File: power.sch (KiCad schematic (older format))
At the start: 29 parts, among them J11 Conn_01x02_Male, U8 TPS63031

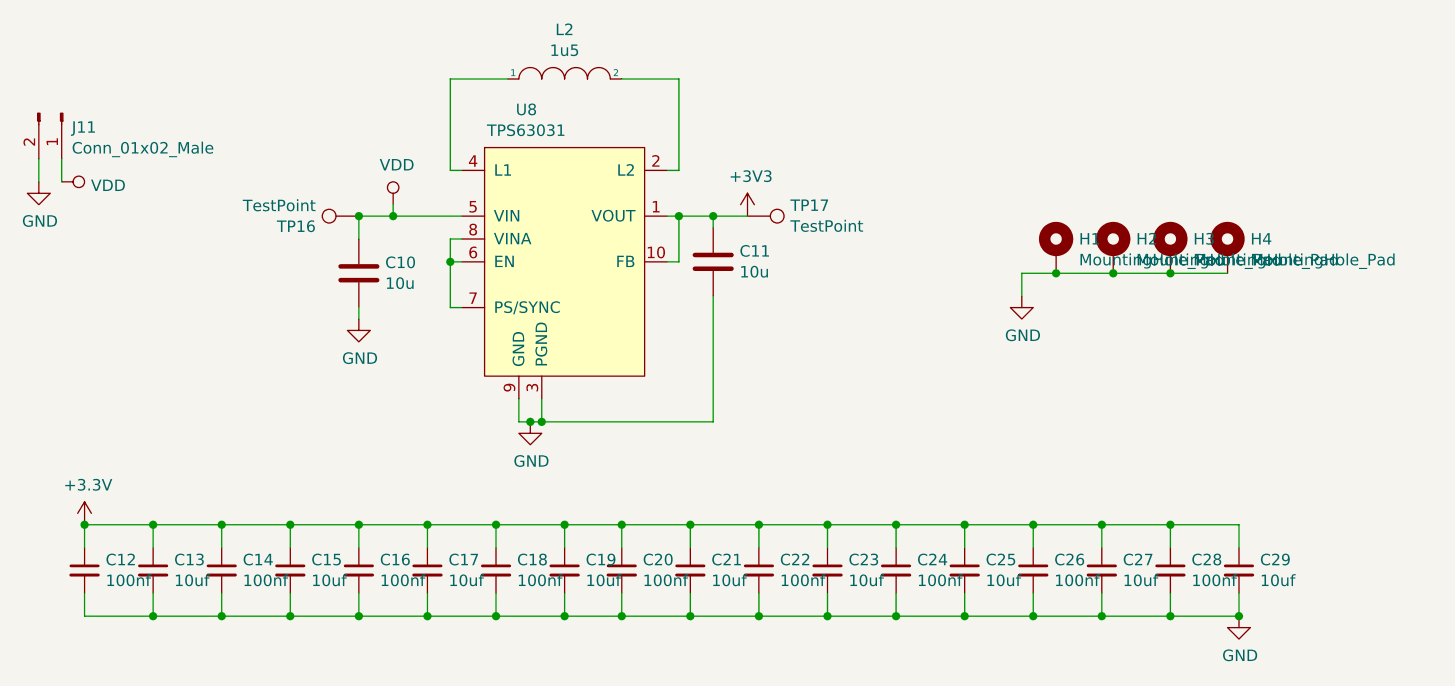
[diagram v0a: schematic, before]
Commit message: Fixed power stage (rev2)
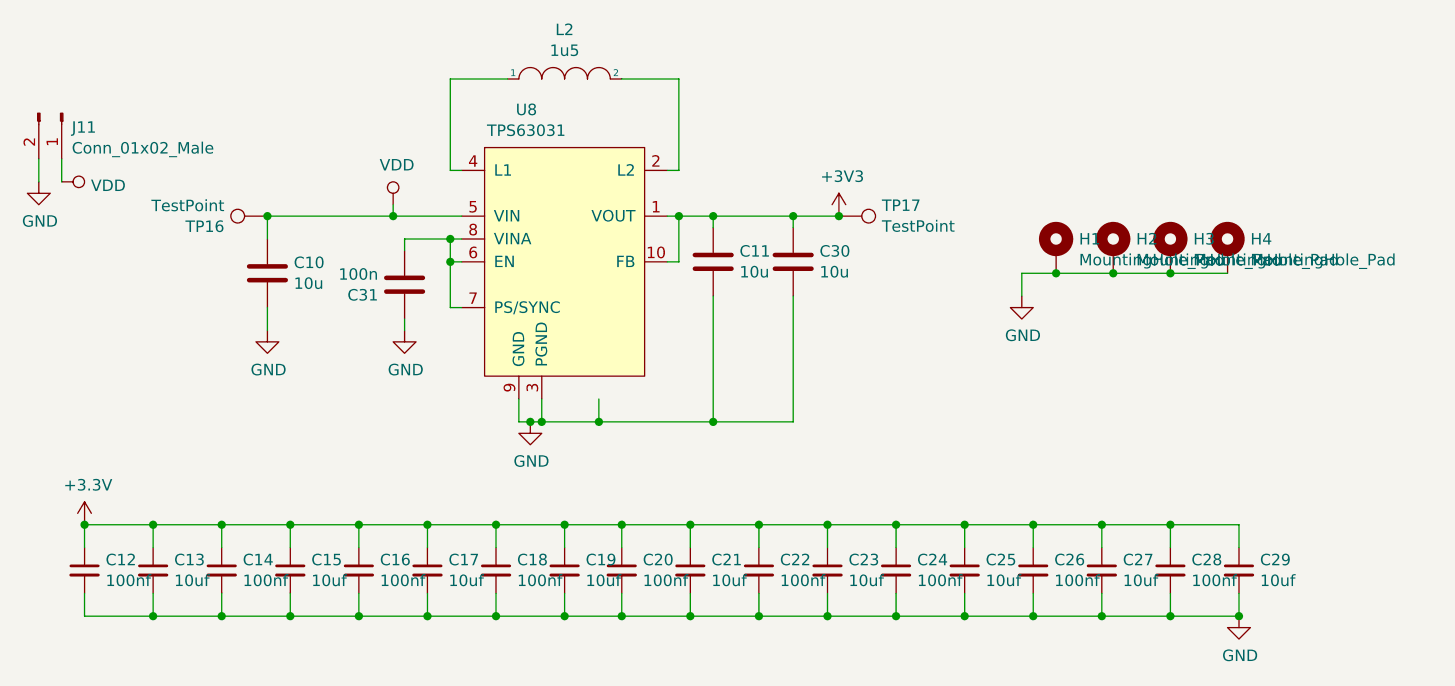
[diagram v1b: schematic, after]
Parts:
- added C30: 10u, Capacitor_SMD:C_0603_1608Metric, symbol Device:C
- added C31: 100n, Capacitor_SMD:C_0603_1608Metric, symbol Device:C
- C10, C11: footprint Capacitor_SMD:CP_Elec_4x5.4 -> Capacitor_SMD:C_0603_1608Metric
- J11: footprint Connector_JST:JST_PH_B2B-PH-K_1x02_P2.00mm_Vertical -> Connector_JST:JST_PH_S2B-PH-K_1x02_P2.00mm_Horizontal
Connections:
- net +3V3: now also C30.1
- net GND: now also C30.2, C31.1
- net at U8.6 (EN), U8.7 (PS/SYNC), U8.8 (VINA): now also C31.2
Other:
- moved on the sheet: C10, TP16, TP17
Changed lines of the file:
@@
 EESchema Schematic File Version 4
+LIBS:Mainboard-cache
 EELAYER 30 0
 EELAYER END
@@
 L power:+3V3 #PWR052
 U 1 1 5DBA4350
-P 6700 3800
-F 0 "#PWR052" H 6700 3650 50  0001 C CNN
-F 1 "+3V3" H 6715 3973 50  0000 C CNN
-F 2 "" H 6700 3800 50  0001 C CNN
-F 3 "" H 6700 3800 50  0001 C CNN
-	1    6700 3800
+P 7100 3800
+F 0 "#PWR052" H 7100 3650 50  0001 C CNN
+F 1 "+3V3" H 7115 3973 50  0000 C CNN
+F 2 "" H 7100 3800 50  0001 C CNN
+F 3 "" H 7100 3800 50  0001 C CNN
+	1    7100 3800
 	1    0    0    -1
 $EndComp
@@
 F 0 "C11" H 6665 4046 50  0000 L CNN
 F 1 "10u" H 6665 3955 50  0000 L CNN
-F 2 "Capacitor_SMD:CP_Elec_4x5.4" H 6588 3850 50  0001 C CNN
+F 2 "Capacitor_SMD:C_0603_1608Metric" H 6588 3850 50  0001 C CNN
 F 3 "~" H 6550 4000 50  0001 C CNN
 	1    6550 4000
@@
 Connection ~ 6550 3800
 Wire Wire Line
-	6550 3800 6700 3800
+	6550 3800 6900 3800
 Wire Wire Line
 	6350 3600 6400 3600
@@
 Connection ~ 5800 4700
 Wire Wire Line
-	5800 4700 6550 4700
+	5800 4700 6050 4700
 $Comp
 L power:GND #PWR051
@@
 L power:GND #PWR050
 U 1 1 5DBBE1E1
-P 5000 4250
-F 0 "#PWR050" H 5000 4000 50  0001 C CNN
-F 1 "GND" H 5005 4077 50  0000 C CNN
-F 2 "" H 5000 4250 50  0001 C CNN
-F 3 "" H 5000 4250 50  0001 C CNN
-	1    5000 4250
+P 4600 4300
+F 0 "#PWR050" H 4600 4050 50  0001 C CNN
+F 1 "GND" H 4605 4127 50  0000 C CNN
+F 2 "" H 4600 4300 50  0001 C CNN
+F 3 "" H 4600 4300 50  0001 C CNN
+	1    4600 4300
 	1    0    0    -1
 $EndComp
@@
 L Device:C C10
 U 1 1 5DBCE6FA
-P 5000 4050
-F 0 "C10" H 5115 4096 50  0000 L CNN
-F 1 "10u" H 5115 4005 50  0000 L CNN
-F 2 "Capacitor_SMD:CP_Elec_4x5.4" H 5038 3900 50  0001 C CNN
-F 3 "~" H 5000 4050 50  0001 C CNN
-	1    5000 4050
-	1    0    0    -1
-$EndComp
-Wire Wire Line
-	5000 4200 5000 4250
-Wire Wire Line
-	5000 3900 5000 3800
-Connection ~ 5000 3800
-Wire Wire Line
-	5000 3800 5150 3800
+P 4600 4050
+F 0 "C10" H 4715 4096 50  0000 L CNN
+F 1 "10u" H 4715 4005 50  0000 L CNN
+F 2 "Capacitor_SMD:C_0603_1608Metric" H 4638 3900 50  0001 C CNN
+F 3 "~" H 4600 4050 50  0001 C CNN
+	1    4600 4050
+	1    0    0    -1
+$EndComp
+Wire Wire Line
+	4600 4200 4600 4300
+Wire Wire Line
+	4600 3900 4600 3800
+Connection ~ 4600 3800
+Wire Wire Line
+	4600 3800 5150 3800
 Wire Wire Line
 	6550 4150 6550 4700
-$Comp
-L Mainboard-rescue:TPS63031-iclr U8
-U 1 1 5DE04FA4
-P 5900 4000
-F 0 "U8" H 5733 4665 50  0000 C CNN
-F 1 "TPS63031" H 5733 4574 50  0000 C CNN
-F 2 "iclr-hw:VSON-10-1EP_2.5x2.5mm_Pitch0.5mm_ThermalPad" H 5900 4600 50  0001 C CNN
-F 3 "" H 5900 4600 50  0001 C CNN
-	1    5900 4000
-	1    0    0    -1
-$EndComp
 $Comp
 L Device:C_Small C?
@@
 L Connector:TestPoint TP?
 U 1 1 5E403DEA
-P 5000 3800
+P 4600 3800
 AR Path="/5E403DEA" Ref="TP?"  Part="1"
 AR Path="/5DB9F80E/5E403DEA" Ref="TP16"  Part="1"
-F 0 "TP16" V 4954 3988 50  0000 L CNN
-F 1 "TestPoint" V 5045 3988 50  0000 L CNN
-F 2 "TestPoint:TestPoint_THTPad_1.0x1.0mm_Drill0.5mm" H 5200 3800 50  0001 C CNN
-F 3 "~" H 5200 3800 50  0001 C CNN
-	1    5000 3800
+F 0 "TP16" V 4554 3988 50  0000 L CNN
+F 1 "TestPoint" V 4645 3988 50  0000 L CNN
+F 2 "TestPoint:TestPoint_THTPad_1.0x1.0mm_Drill0.5mm" H 4800 3800 50  0001 C CNN
+F 3 "~" H 4800 3800 50  0001 C CNN
+	1    4600 3800
 	0    -1   -1   0
 $EndComp
@@
 L Connector:TestPoint TP?
 U 1 1 5E4076DE
-P 6700 3800
+P 7100 3800
 AR Path="/5E4076DE" Ref="TP?"  Part="1"
 AR Path="/5DB9F80E/5E4076DE" Ref="TP17"  Part="1"
-F 0 "TP17" V 6654 3988 50  0000 L CNN
-F 1 "TestPoint" V 6745 3988 50  0000 L CNN
-F 2 "TestPoint:TestPoint_THTPad_1.0x1.0mm_Drill0.5mm" H 6900 3800 50  0001 C CNN
-F 3 "~" H 6900 3800 50  0001 C CNN
-	1    6700 3800
+F 0 "TP17" V 7054 3988 50  0000 L CNN
+F 1 "TestPoint" V 7145 3988 50  0000 L CNN
+F 2 "TestPoint:TestPoint_THTPad_1.0x1.0mm_Drill0.5mm" H 7300 3800 50  0001 C CNN
+F 3 "~" H 7300 3800 50  0001 C CNN
+	1    7100 3800
 	0    1    1    0
 $EndComp
@@
 F 0 "J11" V 3762 3394 50  0000 L CNN
 F 1 "Conn_01x02_Male" V 3853 3394 50  0000 L CNN
-F 2 "Connector_JST:JST_PH_B2B-PH-K_1x02_P2.00mm_Vertical" H 3700 3350 50  0001 C CNN
+F 2 "Connector_JST:JST_PH_S2B-PH-K_1x02_P2.00mm_Horizontal" H 3700 3350 50  0001 C CNN
 F 3 "~" H 3700 3350 50  0001 C CNN
 	1    3700 3350
@@
 Wire Wire Line
 	5150 3800 5450 3800
+Connection ~ 7100 3800
+$Comp
+L Device:C C30
+U 1 1 5E2A869F
+P 6900 4000
+F 0 "C30" H 7015 4046 50  0000 L CNN
+F 1 "10u" H 7015 3955 50  0000 L CNN
+F 2 "Capacitor_SMD:C_0603_1608Metric" H 6938 3850 50  0001 C CNN
+F 3 "~" H 6900 4000 50  0001 C CNN
+	1    6900 4000
+	1    0    0    -1
+$EndComp
+Wire Wire Line
+	6900 3850 6900 3800
+Connection ~ 6900 3800
+Wire Wire Line
+	6900 3800 7100 3800
+Wire Wire Line
+	6550 4700 6900 4700
+Wire Wire Line
+	6900 4700 6900 4150
+Connection ~ 6550 4700
+$Comp
+L Device:C C31
+U 1 1 5E2B517B
+P 5200 4100
+F 0 "C31" H 5315 4146 50  0000 L CNN
+F 1 "100n" H 5315 4055 50  0000 L CNN
+F 2 "Capacitor_SMD:C_0603_1608Metric" H 5238 3950 50  0001 C CNN
+F 3 "~" H 5200 4100 50  0001 C CNN
+	1    5200 4100
+	-1   0    0    1
+$EndComp
+$Comp
+L Mainboard-rescue:TPS63031-iclr U8
+U 1 1 5DE04FA4
+P 5900 4000
+F 0 "U8" H 5733 4665 50  0000 C CNN
+F 1 "TPS63031" H 5733 4574 50  0000 C CNN
+F 2 "iclr-hw:VSON-10-1EP_2.5x2.5mm_Pitch0.5mm_ThermalPad" H 5900 4600 50  0001 C CNN
+F 3 "" H 5900 4600 50  0001 C CNN
+	1    5900 4000
+	1    0    0    -1
+$EndComp
+Wire Wire Line
+	5200 3950 5200 3900
+Wire Wire Line
+	5200 3900 5400 3900
+Connection ~ 5400 3900
+$Comp
+L power:GND #PWR0109
+U 1 1 5E2C5248
+P 5200 4300
+F 0 "#PWR0109" H 5200 4050 50  0001 C CNN
+F 1 "GND" H 5205 4127 50  0000 C CNN
+F 2 "" H 5200 4300 50  0001 C CNN
+F 3 "" H 5200 4300 50  0001 C CNN
+	1    5200 4300
+	1    0    0    -1
+$EndComp
+Wire Wire Line
+	5200 4300 5200 4250
+Wire Wire Line
+	6050 4600 6050 4700
+Connection ~ 6050 4700
+Wire Wire Line
+	6050 4700 6550 4700
 $EndSCHEMATC

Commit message: hardest commit of my life
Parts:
- C10, C11, C30: value 10u -> 10uF
- C12, C14, C16, C18, C20, C22, C24, C26, C28: value 100nf -> 100nF
- C13, C15, C17, C19, C21, C23, C25, C27, C29: value 10uf -> 10uF
- C31: value 100n -> 100nF
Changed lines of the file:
@@
 EESchema Schematic File Version 4
-LIBS:Mainboard-cache
 EELAYER 30 0
 EELAYER END
@@
 P 6550 4000
 F 0 "C11" H 6665 4046 50  0000 L CNN
-F 1 "10u" H 6665 3955 50  0000 L CNN
+F 1 "10uF" H 6665 3955 50  0000 L CNN
 F 2 "Capacitor_SMD:C_0603_1608Metric" H 6588 3850 50  0001 C CNN
 F 3 "~" H 6550 4000 50  0001 C CNN
@@
 P 4600 4050
 F 0 "C10" H 4715 4096 50  0000 L CNN
-F 1 "10u" H 4715 4005 50  0000 L CNN
+F 1 "10uF" H 4715 4005 50  0000 L CNN
 F 2 "Capacitor_SMD:C_0603_1608Metric" H 4638 3900 50  0001 C CNN
 F 3 "~" H 4600 4050 50  0001 C CNN
@@
 AR Path="/5DB9F80E/5E076608" Ref="C13"  Part="1"
 F 0 "C13" H 4192 5396 50  0000 L CNN
-F 1 "10uf" H 4192 5305 50  0000 L CNN
+F 1 "10uF" H 4192 5305 50  0000 L CNN
 F 2 "Capacitor_SMD:C_0603_1608Metric" H 4100 5350 50  0001 C CNN
 F 3 "~" H 4100 5350 50  0001 C CNN
@@
 AR Path="/5DB9F80E/5E07660E" Ref="C12"  Part="1"
 F 0 "C12" H 3892 5396 50  0000 L CNN
-F 1 "100nf" H 3892 5305 50  0000 L CNN
+F 1 "100nF" H 3892 5305 50  0000 L CNN
 F 2 "Capacitor_SMD:C_0603_1608Metric" H 3800 5350 50  0001 C CNN
 F 3 "~" H 3800 5350 50  0001 C CNN
@@
 AR Path="/5DB9F80E/5E078029" Ref="C15"  Part="1"
 F 0 "C15" H 4792 5396 50  0000 L CNN
-F 1 "10uf" H 4792 5305 50  0000 L CNN
+F 1 "10uF" H 4792 5305 50  0000 L CNN
 F 2 "Capacitor_SMD:C_0603_1608Metric" H 4700 5350 50  0001 C CNN
 F 3 "~" H 4700 5350 50  0001 C CNN
@@
 AR Path="/5DB9F80E/5E07802F" Ref="C14"  Part="1"
 F 0 "C14" H 4492 5396 50  0000 L CNN
-F 1 "100nf" H 4492 5305 50  0000 L CNN
+F 1 "100nF" H 4492 5305 50  0000 L CNN
 F 2 "Capacitor_SMD:C_0603_1608Metric" H 4400 5350 50  0001 C CNN
 F 3 "~" H 4400 5350 50  0001 C CNN
@@
 AR Path="/5DB9F80E/5E07D75B" Ref="C17"  Part="1"
 F 0 "C17" H 5392 5396 50  0000 L CNN
-F 1 "10uf" H 5392 5305 50  0000 L CNN
+F 1 "10uF" H 5392 5305 50  0000 L CNN
 F 2 "Capacitor_SMD:C_0603_1608Metric" H 5300 5350 50  0001 C CNN
 F 3 "~" H 5300 5350 50  0001 C CNN
@@
 AR Path="/5DB9F80E/5E07D761" Ref="C16"  Part="1"
 F 0 "C16" H 5092 5396 50  0000 L CNN
-F 1 "100nf" H 5092 5305 50  0000 L CNN
+F 1 "100nF" H 5092 5305 50  0000 L CNN
 F 2 "Capacitor_SMD:C_0603_1608Metric" H 5000 5350 50  0001 C CNN
 F 3 "~" H 5000 5350 50  0001 C CNN
@@
 AR Path="/5DB9F80E/5E07D77F" Ref="C19"  Part="1"
 F 0 "C19" H 5992 5396 50  0000 L CNN
-F 1 "10uf" H 5992 5305 50  0000 L CNN
+F 1 "10uF" H 5992 5305 50  0000 L CNN
 F 2 "Capacitor_SMD:C_0603_1608Metric" H 5900 5350 50  0001 C CNN
 F 3 "~" H 5900 5350 50  0001 C CNN
@@
 AR Path="/5DB9F80E/5E07D785" Ref="C18"  Part="1"
 F 0 "C18" H 5692 5396 50  0000 L CNN
-F 1 "100nf" H 5692 5305 50  0000 L CNN
+F 1 "100nF" H 5692 5305 50  0000 L CNN
 F 2 "Capacitor_SMD:C_0603_1608Metric" H 5600 5350 50  0001 C CNN
 F 3 "~" H 5600 5350 50  0001 C CNN
@@
 AR Path="/5DB9F80E/5E08499D" Ref="C21"  Part="1"
 F 0 "C21" H 6542 5396 50  0000 L CNN
-F 1 "10uf" H 6542 5305 50  0000 L CNN
+F 1 "10uF" H 6542 5305 50  0000 L CNN
 F 2 "Capacitor_SMD:C_0603_1608Metric" H 6450 5350 50  0001 C CNN
 F 3 "~" H 6450 5350 50  0001 C CNN
@@
 AR Path="/5DB9F80E/5E0849A3" Ref="C20"  Part="1"
 F 0 "C20" H 6242 5396 50  0000 L CNN
-F 1 "100nf" H 6242 5305 50  0000 L CNN
+F 1 "100nF" H 6242 5305 50  0000 L CNN
 F 2 "Capacitor_SMD:C_0603_1608Metric" H 6150 5350 50  0001 C CNN
 F 3 "~" H 6150 5350 50  0001 C CNN
@@
 AR Path="/5DB9F80E/5E0849C1" Ref="C23"  Part="1"
 F 0 "C23" H 7142 5396 50  0000 L CNN
-F 1 "10uf" H 7142 5305 50  0000 L CNN
+F 1 "10uF" H 7142 5305 50  0000 L CNN
 F 2 "Capacitor_SMD:C_0603_1608Metric" H 7050 5350 50  0001 C CNN
 F 3 "~" H 7050 5350 50  0001 C CNN
@@
 AR Path="/5DB9F80E/5E0849C7" Ref="C22"  Part="1"
 F 0 "C22" H 6842 5396 50  0000 L CNN
-F 1 "100nf" H 6842 5305 50  0000 L CNN
+F 1 "100nF" H 6842 5305 50  0000 L CNN
 F 2 "Capacitor_SMD:C_0603_1608Metric" H 6750 5350 50  0001 C CNN
 F 3 "~" H 6750 5350 50  0001 C CNN
@@
 AR Path="/5DB9F80E/5E0849E5" Ref="C25"  Part="1"
 F 0 "C25" H 7742 5396 50  0000 L CNN
-F 1 "10uf" H 7742 5305 50  0000 L CNN
+F 1 "10uF" H 7742 5305 50  0000 L CNN
 F 2 "Capacitor_SMD:C_0603_1608Metric" H 7650 5350 50  0001 C CNN
 F 3 "~" H 7650 5350 50  0001 C CNN
@@
 AR Path="/5DB9F80E/5E0849EB" Ref="C24"  Part="1"
 F 0 "C24" H 7442 5396 50  0000 L CNN
-F 1 "100nf" H 7442 5305 50  0000 L CNN
+F 1 "100nF" H 7442 5305 50  0000 L CNN
 F 2 "Capacitor_SMD:C_0603_1608Metric" H 7350 5350 50  0001 C CNN
 F 3 "~" H 7350 5350 50  0001 C CNN
@@
 AR Path="/5DB9F80E/5E084A09" Ref="C27"  Part="1"
 F 0 "C27" H 8342 5396 50  0000 L CNN
-F 1 "10uf" H 8342 5305 50  0000 L CNN
+F 1 "10uF" H 8342 5305 50  0000 L CNN
 F 2 "Capacitor_SMD:C_0603_1608Metric" H 8250 5350 50  0001 C CNN
 F 3 "~" H 8250 5350 50  0001 C CNN
@@
 AR Path="/5DB9F80E/5E084A0F" Ref="C26"  Part="1"
 F 0 "C26" H 8042 5396 50  0000 L CNN
-F 1 "100nf" H 8042 5305 50  0000 L CNN
+F 1 "100nF" H 8042 5305 50  0000 L CNN
 F 2 "Capacitor_SMD:C_0603_1608Metric" H 7950 5350 50  0001 C CNN
 F 3 "~" H 7950 5350 50  0001 C CNN
@@
 AR Path="/5DB9F80E/5E153428" Ref="C29"  Part="1"
 F 0 "C29" H 8942 5396 50  0000 L CNN
-F 1 "10uf" H 8942 5305 50  0000 L CNN
+F 1 "10uF" H 8942 5305 50  0000 L CNN
 F 2 "Capacitor_SMD:C_0603_1608Metric" H 8850 5350 50  0001 C CNN
 F 3 "~" H 8850 5350 50  0001 C CNN
@@
 AR Path="/5DB9F80E/5E15342E" Ref="C28"  Part="1"
 F 0 "C28" H 8642 5396 50  0000 L CNN
-F 1 "100nf" H 8642 5305 50  0000 L CNN
+F 1 "100nF" H 8642 5305 50  0000 L CNN
 F 2 "Capacitor_SMD:C_0603_1608Metric" H 8550 5350 50  0001 C CNN
 F 3 "~" H 8550 5350 50  0001 C CNN
@@
 P 6900 4000
 F 0 "C30" H 7015 4046 50  0000 L CNN
-F 1 "10u" H 7015 3955 50  0000 L CNN
+F 1 "10uF" H 7015 3955 50  0000 L CNN
 F 2 "Capacitor_SMD:C_0603_1608Metric" H 6938 3850 50  0001 C CNN
 F 3 "~" H 6900 4000 50  0001 C CNN
@@
 P 5200 4100
 F 0 "C31" H 5315 4146 50  0000 L CNN
-F 1 "100n" H 5315 4055 50  0000 L CNN
+F 1 "100nF" H 5315 4055 50  0000 L CNN
 F 2 "Capacitor_SMD:C_0603_1608Metric" H 5238 3950 50  0001 C CNN
 F 3 "~" H 5200 4100 50  0001 C CNN
